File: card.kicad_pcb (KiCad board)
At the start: 2 copper layers, 38.6 x 52.3 mm, 81 parts, among them J1 Conn_01x20_Male, J2 HDMI_A, J3 Conn_01x20_Male, J4 USB_B_Micro, SW1 SW_DPST_x2, U1 SPX3819-1.8, U2 IMP811REUS-T, U3 SP6205EM5-L-3-3_TR, U4 MP1469GJ, U5 W25Q32JVSS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

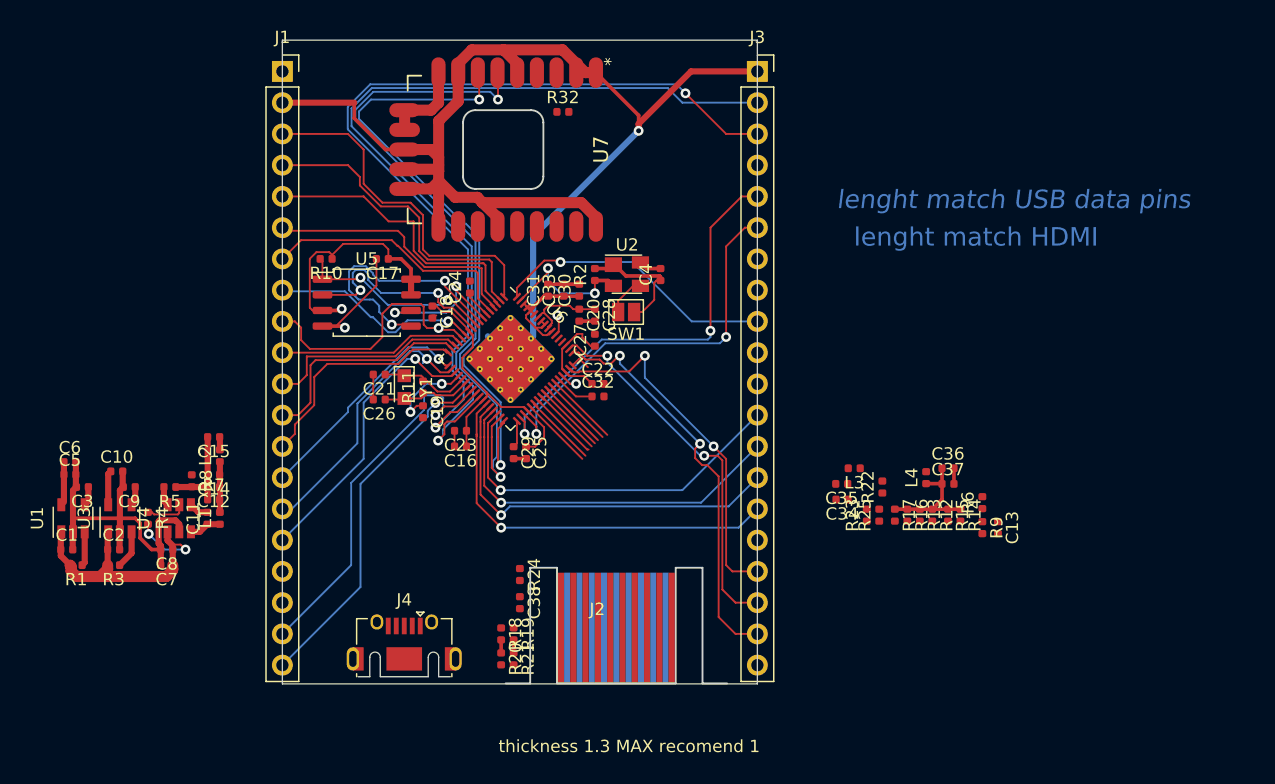
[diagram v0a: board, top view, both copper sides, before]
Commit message: did some routing and fixed some pinouts on components
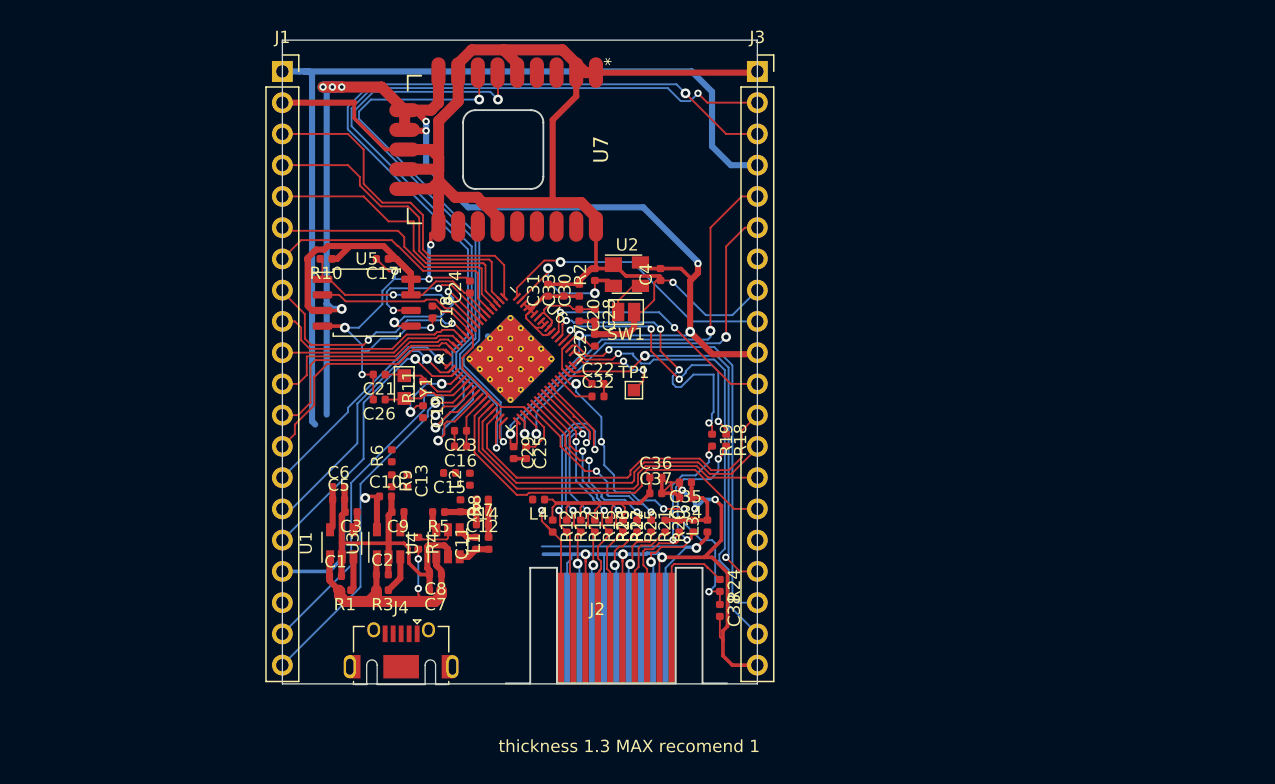
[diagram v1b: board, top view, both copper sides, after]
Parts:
- removed R32: 510R, Resistor_SMD:R_0402_1005Metric
- added TP1: TestPoint, TestPoint:TestPoint_Pad_1.0x1.0mm, F.Cu at (262.5, 85.1)
- moved C13 48.2 mm to (244.1, 92.5)
- moved R6 48.2 mm to (242.8, 90.4)
- moved R9 48.2 mm to (242.8, 92.5)
- moved L4 31.5 mm to (254.8, 94.0), turned to 180 degrees
- moved R14 30.9 mm to (258.2, 96.1)
- moved R12 30.9 mm to (255.9, 96.1)
- moved R13 28.7 mm to (257.0, 96.1)
- moved R15 28.7 mm to (259.3, 96.1)
- moved R16 24.3 mm to (260.5, 96.1)
- moved R18 24.1 mm to (270.0, 89.2)
- moved C36 23.8 mm to (264.3, 92.2)
- moved C37 23.8 mm to (264.3, 93.5)
- moved R19 22.5 mm to (268.9, 89.2)
- moved R17 22.1 mm to (261.6, 96.1)
- moved R4 22.1 mm to (245.0, 97.5)
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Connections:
- U6 pad 51: (no net) -> Net-(TP1-Pad1)
- U7 pad 10: 3V3 -> +3V3
- U7 pad 11: 3V3 -> +3V3
- U7 pad 9: 3V3 -> +3V3
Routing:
- net +3V3: track 44.4 -> 182.8 mm, vias 3 -> 13
- net GND: track 169.5 -> 273.5 mm, vias 2 -> 13
- net +5V: track 25.0 -> 119.1 mm, vias 2 -> 3
- net HDMI_PLG: track 1.41 -> 28.1 mm, vias 1 -> 5
- net HDMI_SCL: track 0.00 -> 23.9 mm, vias 0 -> 4
- net HDMI_SDA: track 0.00 -> 22.4 mm, vias 0 -> 4
- net TX2_N: track 5.84 -> 27.7 mm, vias 0 -> 2
- net Net-(J2-Pad16): track 1.06 -> 22.4 mm, vias 0 -> 3
- net Net-(J2-Pad15): track 1.06 -> 20.8 mm, vias 0 -> 2
- net TX1_P: track 5.78 -> 25.5 mm, vias 0 -> 3
- net PORT20: track 1.79 -> 20.2 mm, vias 1 -> 2
- net TX0_N: track 5.79 -> 23.1 mm, vias 0 -> 2
- net TX1_N: track 5.76 -> 22.2 mm, vias 0 -> 3
- net TX0_P: track 5.78 -> 21.8 mm, vias 0 -> 2
- net Net-(J2-Pad19): track 0.00 -> 9.60 mm
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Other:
- board text removed: "lenght match HDMI"
- board text removed: "lenght match USB data pins"

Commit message: did some work on routing
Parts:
- moved C13 0.30 mm to (244.1, 92.2)
- moved R6 0.30 mm to (242.8, 90.1)
- moved R9 0.30 mm to (242.8, 92.2)
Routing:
- net GND: track 273.5 -> 298.8 mm, vias 13 -> 19
- net +5V: track 119.1 -> 142.3 mm, vias 3 -> 5
- net TX2_P: track 11.0 -> 25.9 mm, vias 1 -> 2
- net +1V1: track 33.8 -> 46.3 mm, vias 0 -> 1
- net +2V5: track 3.29 -> 5.62 mm
- net port15-SDA: track 29.4 -> 30.3 mm
- net port14-SCL: track 31.0 -> 31.7 mm
- net +3V3: track 182.8 -> 183.5 mm
- added copper zone on B.Cu, net GND

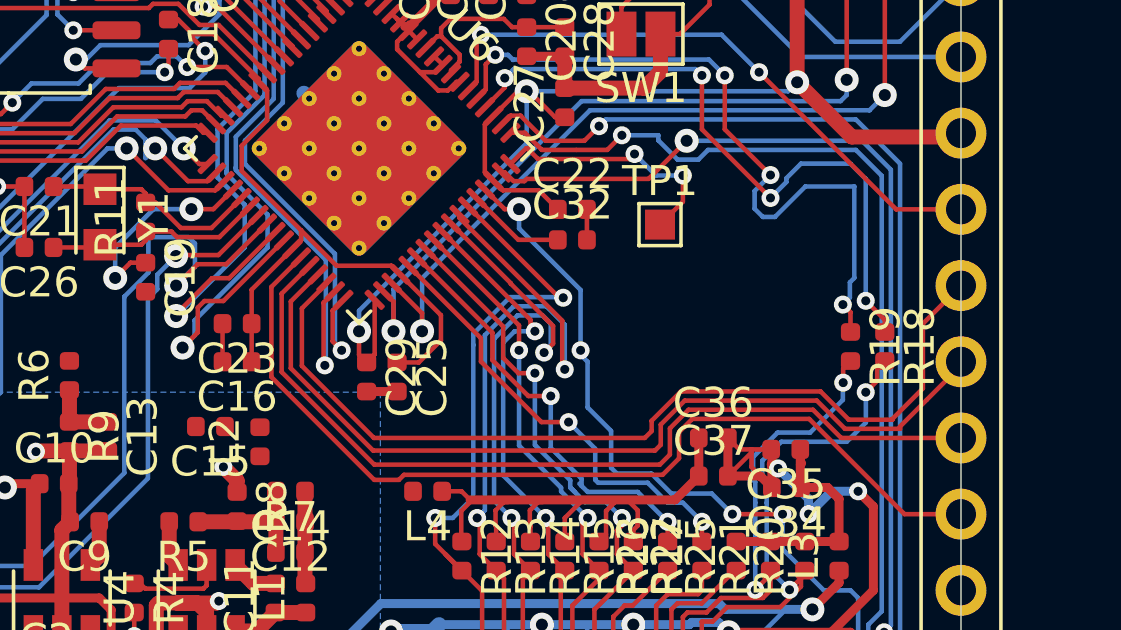
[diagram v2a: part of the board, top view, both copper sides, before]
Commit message: added solder jumpers for optonla blue tooth
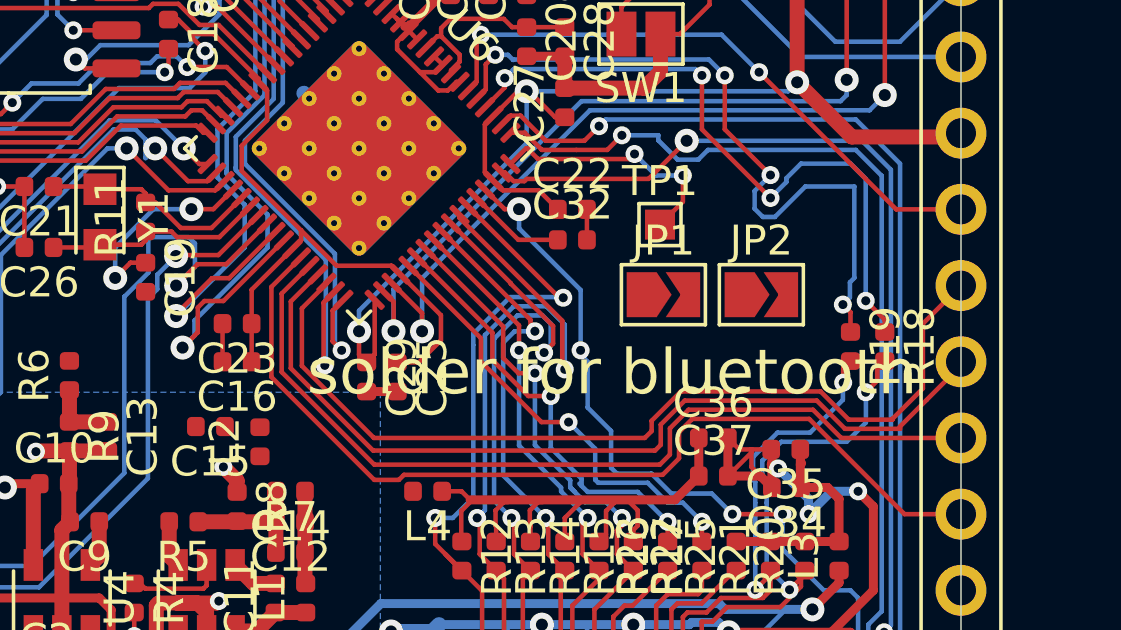
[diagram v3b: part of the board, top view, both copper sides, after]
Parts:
- added JP1: Jumper, Jumper:SolderJumper-2_P1.3mm_Open_TrianglePad1.0x1.5mm, F.Cu at (262.6, 87.4)
- added JP2: Jumper, Jumper:SolderJumper-2_P1.3mm_Open_TrianglePad1.0x1.5mm, F.Cu at (265.9, 87.4)
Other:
- board text added: "solder for bluetooth"

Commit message: did a little bit more routing
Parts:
- moved JP2 12.2 mm to (268.4, 75.5), turned to 180 degrees
- moved JP1 11.1 mm to (268.4, 78.0), turned to 180 degrees
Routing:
- net Net-(JP1-Pad2): track 0.00 -> 24.5 mm, vias 0 -> 2
- net Net-(JP2-Pad2): track 0.00 -> 24.3 mm, vias 0 -> 2
- net +3V3: track 183.5 -> 178.1 mm
- net HOST1_DP: track 34.2 -> 38.9 mm, vias 2 -> 3
- net GND: track 298.8 -> 296.0 mm, vias 19 -> 20
- net /CPU/SPI_CLK: track 12.4 -> 14.8 mm
- net HOST1_DM: track 32.0 -> 34.2 mm
- net HDMI_PLG: track 28.1 -> 29.3 mm, vias 5 -> 6

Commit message: did some more routing
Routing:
- net +2V5: track 5.62 -> 63.1 mm, vias 0 -> 2
- net GND: track 296.0 -> 324.4 mm, vias 20 -> 28
- net +3V3: track 178.1 -> 205.6 mm, vias 13 -> 15
- net +1V1: track 46.3 -> 72.6 mm, vias 1 -> 4
- net +1V8: track 13.8 -> 17.1 mm, vias 0 -> 1
- net Net-(C12-Pad2): track 4.62 -> 7.83 mm
- net VOUT1: track 32.3 -> 33.6 mm, vias 2 -> 4
- net +1V0: track 0.00 -> 1.18 mm
- net Net-(TP1-Pad1): track 8.43 -> 7.61 mm
